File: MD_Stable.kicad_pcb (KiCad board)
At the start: 2 copper layers, 100 x 100 mm, 305 parts, among them J1 Conn_02x04_Counter_Clockwise, J10 Conn_02x06_Odd_Even, J11 Conn_01x08_Pin, J12 Conn_01x05_Socket, J2 XT30_Male, J3 XT60_Male, J4 RE1, J5 RE2, J6 RE3, J7 MO_XT60_Female1, J8 MO_XT60_Female2, J9 MO_XT60_Female3, Q1 TPH4R008QM, Q10 TPH4R008QM, Q11 TPH4R008QM, Q12 TPH4R008QM, Q2 TPH4R008QM, Q3 TPH4R008QM, Q4 TPH4R008QM, Q5 TPH4R008QM, Q6 TPH4R008QM, Q7 TPH4R008QM, Q8 TPH4R008QM, Q9 TPH4R008QM, SW1 SW_Push, SW2 SW_Push, SW3 PWM, SW4 PWM, SW5 PWM, SW6 DIR, SW7 DIR, SW8 DIR, U1 NJM7808SDL1, U10 74AHC1G08W5, U11 74AHC1G08W5, U12 74AHC1G08W5, U13 IRS2302S, U14 IRS2302S, U15 IRS2302S, U16 NE555D, U17 IRS2302S, U18 IRS2302S, U19 IRS2302S, U2 BA05CC0Tに似た何か, U20 74AHC1G08W5, U21 74AHC1G08W5, U22 74AHC1G08W5, U23 UTRS485G-S08-R, U24 UTRS485G-S08-R, U3 STM32G431K8Tx, U4 BA05CC0Tに似た何か, U5 BA033CC0FP, U6 π160M60, U7 74AHC1G04W5, U8 74AHC1G04W5, U9 74AHC1G04W5

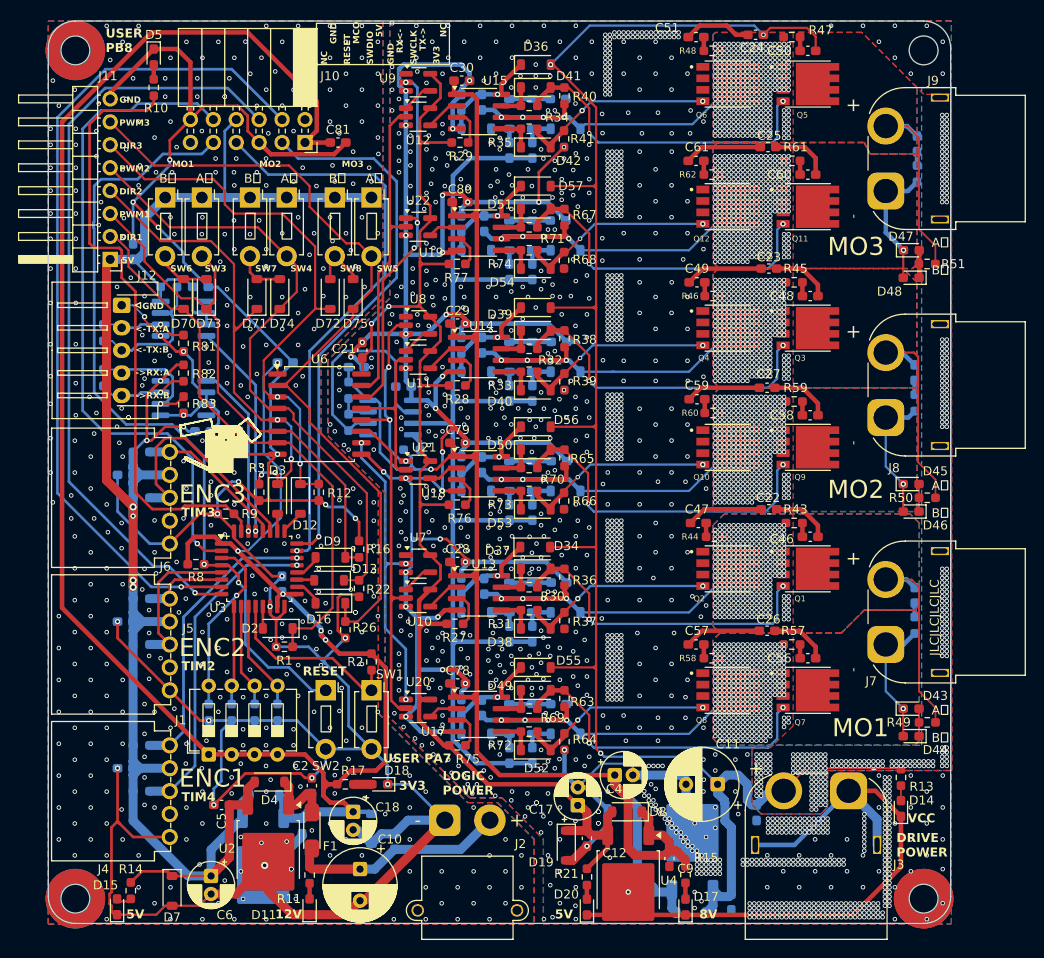
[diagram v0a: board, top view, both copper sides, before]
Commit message: 配線修正
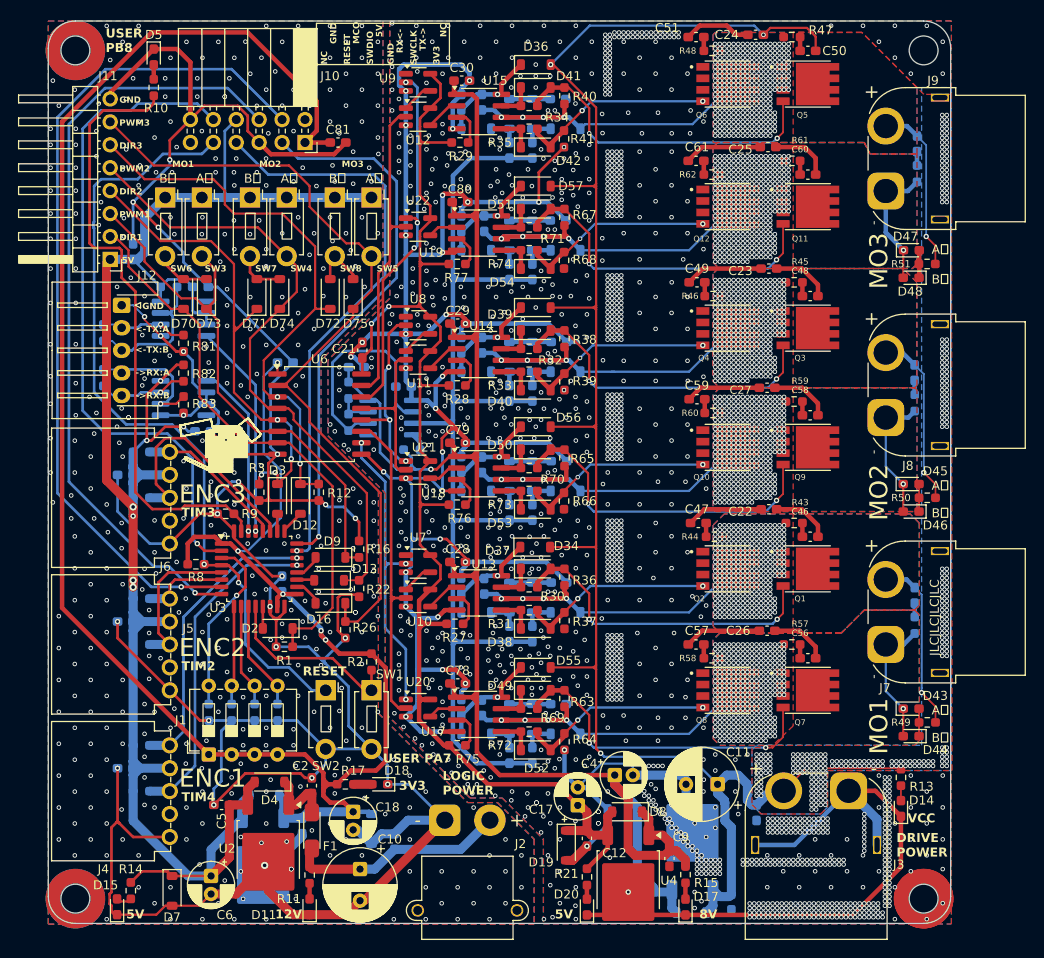
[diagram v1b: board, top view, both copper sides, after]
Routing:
- net Source_2A: track 63.7 -> 59.2 mm, vias 349 -> 342
- net Source_3A: track 62.0 -> 58.1 mm, vias 335 -> 327
- net Source_1A: track 62.5 -> 58.6 mm, vias 324 -> 317
- net Source_3B: vias 376 -> 369
- net Source_2B: vias 363 -> 356

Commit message: RS485Tx fix
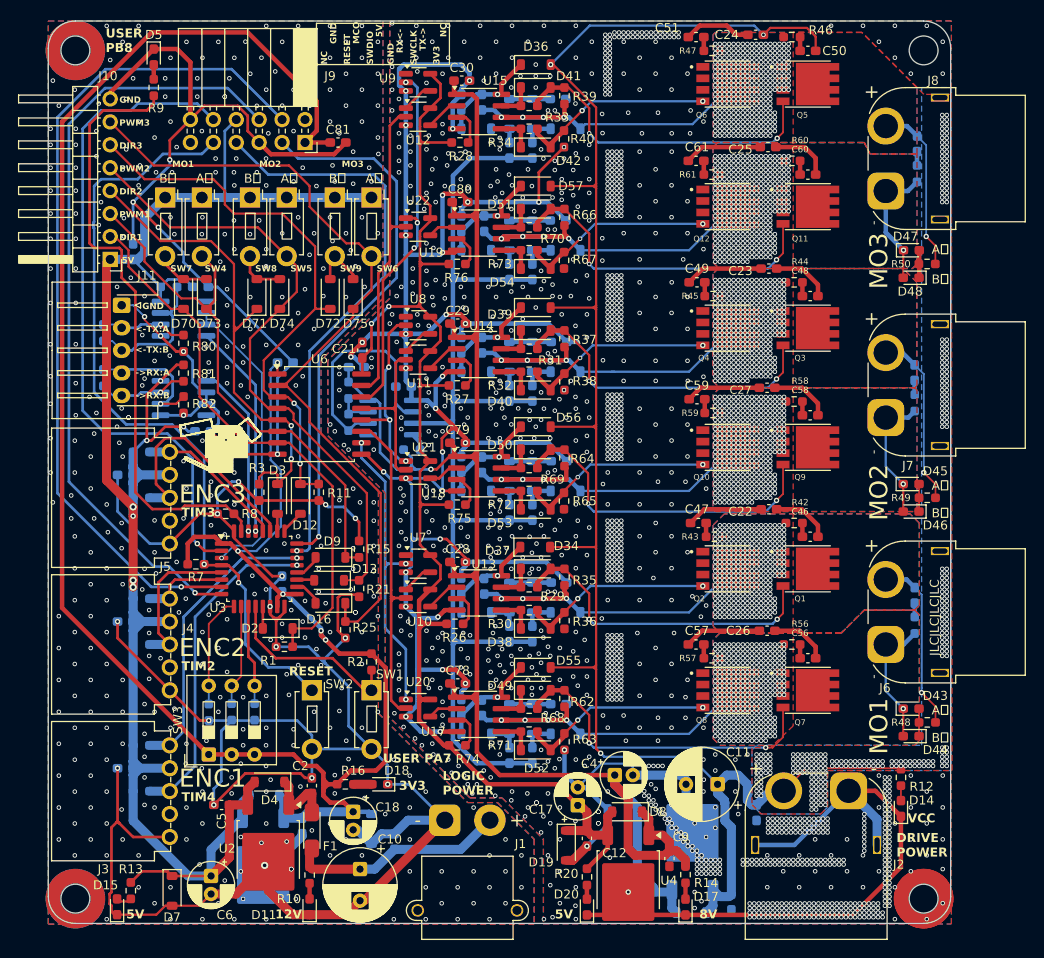
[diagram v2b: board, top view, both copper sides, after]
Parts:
- removed the J1 at (119.4, 132.1)
- removed the R7 at (119.4, 127.4)
- added SW3: SW_DIP_x03, Button_Switch_THT:SW_DIP_SPSTx03_Slide_9.78x9.8mm_W7.62mm_P2.54mm, F.Cu at (119.4, 132.1)
- moved R4 2.54 mm to (124.5, 127.4)
- moved R5 2.54 mm to (121.9, 127.4)
- moved R6 2.54 mm to (119.4, 127.4)
- moved SW2 1.52 mm to (130.8, 125.0)
- renumbered C84 to C82, C82 to C83, C83 to C84, J2 to J1, J11 to J10, J12 to J11, J3 to J2, J4 to J3, J5 to J4, J6 to J5, J7 to J6, J8 to J7, J9 to J8, J10 to J9, R11 to R10, R12 to R11, R13 to R12, R14 to R13, R15 to R14, R16 to R15, R17 to R16, R18 to R17, R19 to R18, R20 to R19, R21 to R20, R22 to R21, R23 to R22, R24 to R23, R25 to R24, R26 to R25, R27 to R26, R28 to R27, R29 to R28, R30 to R29, R31 to R30, R32 to R31, R33 to R32, R34 to R33, R35 to R34, R36 to R35, R37 to R36, R38 to R37, R39 to R38, R40 to R39, R41 to R40, R42 to R41, R43 to R42, R44 to R43, R45 to R44, R46 to R45, R47 to R46, R48 to R47, R49 to R48, R50 to R49, R51 to R50, R52 to R51, R53 to R52, R54 to R53, R55 to R54, R56 to R55, R57 to R56, R58 to R57, R59 to R58, R60 to R59, R61 to R60, R62 to R61, R63 to R62, R64 to R63, R65 to R64, R66 to R65, R67 to R66, R68 to R67, R69 to R68, R70 to R69, R8 to R7, R71 to R70, R72 to R71, R73 to R72, R74 to R73, R75 to R74, R76 to R75, R77 to R76, R78 to R77, R79 to R78, R80 to R79, R9 to R8, R81 to R80, R82 to R81, R83 to R82, R10 to R9, SW3 to SW4, SW4 to SW5, SW5 to SW6, SW6 to SW7, SW7 to SW8, SW8 to SW9
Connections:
- J1 pad : (no net) -> GNDD
- U23 pad 2: +5VD -> RS485_DE
- U23 pad 3: +5VD -> RS485_DE
- U3 pad 3: DIP_4 -> RS485_DE
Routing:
- net RS485_DE: track 0.00 -> 33.7 mm, vias 0 -> 1
- net DIP_4: track 19.8 -> 0.00 mm, vias 1 -> 0
- net GNDD: track 390.8 -> 384.1 mm, vias 445 -> 442
- net +5VD: track 216.2 -> 210.2 mm
- net DIP_3: track 10.9 -> 12.5 mm
- net RESET: track 88.5 -> 87.0 mm
- net DIP_1: track 12.1 -> 11.0 mm
- net DIR2: vias 4 -> 2
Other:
- board text added: "DCMotor Driver Rev3.2 @KayOChef_meme"
- board text removed: "DCMotor Driver Rev3.1 @KayOChef_meme"

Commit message: beyond the MD10C Rev4.0
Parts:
- Q1, Q10, Q11, Q12, Q2, Q3, Q4, Q5, Q6, Q7, Q8, Q9: value TPH4R008QM -> AGM028N08A; footprint MyLib:8-SOP Advance (5x5.75) -> Package_DFN_QFN:PQFN-8-EP_6x5mm_P1.27mm_Generic
- U1: value NJM7808SDL1 -> NJM7815SDL1
- U13, U14, U15, U17, U18, U19: value IRS2302S -> IR2184
- moved C28 8.24 mm to (151.5, 117.6), turned to 180 degrees
- moved C78 8.24 mm to (151.5, 131.1), turned to 180 degrees
- moved C79 8.19 mm to (151.0, 104.6), turned to 180 degrees
- moved C29 8.10 mm to (151.3, 91.2), turned to 180 degrees
- moved C80 7.97 mm to (151.3, 77.7), turned to 180 degrees
- moved C30 7.87 mm to (151.3, 64.3), turned to 180 degrees
- moved R28 3.56 mm to (143.7, 64.3)
- moved R27 3.25 mm to (143.7, 91.2)
- moved R75 3.25 mm to (143.7, 104.4)
- moved R76 3.25 mm to (143.7, 77.7)
- moved R26 3.00 mm to (143.7, 117.6)
- moved C23 0.76 mm to (180.7, 78.2)
- moved C25 0.66 mm to (180.7, 64.8)
- moved C26 0.56 mm to (180.7, 118.4)
- moved C27 0.56 mm to (180.7, 91.4)
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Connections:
- C28 pad 1: +8V -> +15V
- C29 pad 1: +8V -> +15V
- C3 pad 1: +8V -> +15V
- C30 pad 1: +8V -> +15V
- C4 pad 1: +8V -> +15V
- C62 pad 1: +8V -> +15V
- C78 pad 1: +8V -> +15V
- C79 pad 1: +8V -> +15V
- C80 pad 1: +8V -> +15V
- C9 pad 1: +8V -> +15V
- D1 pad 2: +8V -> +15V
- D6 pad 1: +8V -> +15V
- D8 pad 1: +8V -> +15V
- R14 pad 2: +8V -> +15V
- R41 pad 1: +8V -> +15V
- R54 pad 1: +8V -> +15V
- U1 pad 3: +8V -> +15V
- U13 pad 1: +8V -> Net-(U10A-Y)
- U13 pad 2: Net-(U10A-Y) -> Net-(U13-~{SD})
- U13 pad 3: Net-(U13-~{SD}) -> GND
- U13 pad 4: GND -> Net-(D38-K)
- U13 pad 5: Net-(D38-K) -> +15V
- U14 pad 1: +8V -> Net-(U11A-Y)
- U14 pad 2: Net-(U11A-Y) -> Net-(U14-~{SD})
- U14 pad 3: Net-(U14-~{SD}) -> GND
- U14 pad 4: GND -> Net-(D40-K)
- U14 pad 5: Net-(D40-K) -> +15V
- U15 pad 1: +8V -> Net-(U12A-Y)
- U15 pad 2: Net-(U12A-Y) -> Net-(U15-~{SD})
- U15 pad 3: Net-(U15-~{SD}) -> GND
- U15 pad 4: GND -> Net-(D42-K)
- U15 pad 5: Net-(D42-K) -> +15V
- U16 pad 8: +8V -> +15V
- U17 pad 1: +8V -> Net-(U17-IN)
- U17 pad 2: Net-(U17-IN) -> Net-(U17-~{SD})
- U17 pad 3: Net-(U17-~{SD}) -> GND
- U17 pad 4: GND -> Net-(D52-K)
- U17 pad 5: Net-(D52-K) -> +15V
- U18 pad 1: +8V -> Net-(U18-IN)
- U18 pad 2: Net-(U18-IN) -> Net-(U18-~{SD})
- U18 pad 3: Net-(U18-~{SD}) -> GND
- U18 pad 4: GND -> Net-(D53-K)
- U18 pad 5: Net-(D53-K) -> +15V
- U19 pad 1: +8V -> Net-(U19-IN)
- U19 pad 2: Net-(U19-IN) -> Net-(U19-~{SD})
- U19 pad 3: Net-(U19-~{SD}) -> GND
- U19 pad 4: GND -> Net-(D54-K)
- U19 pad 5: Net-(D54-K) -> +15V
- U4 pad 1: +8V -> +15V
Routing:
- net +15V: track 0.00 -> 247.3 mm, vias 0 -> 14
- net +8V: track 188.8 -> 0.00 mm, vias 1 -> 0
- net GND: track 402.6 -> 320.9 mm, vias 1305 -> 1261
- net +5V: track 150.8 -> 135.1 mm
- net Net-(D52-K): track 4.19 -> 11.3 mm
- net Net-(D54-K): track 4.19 -> 11.2 mm
- net Net-(D38-K): track 4.19 -> 11.0 mm
- net Net-(D53-K): track 4.19 -> 10.9 mm
- net Net-(D42-K): track 4.19 -> 10.7 mm
- net Net-(D40-K): track 4.19 -> 10.5 mm
- net VCC: track 231.4 -> 235.2 mm
- net 555_Out_A: track 126.3 -> 130.0 mm
- net Net-(U18-~{SD}): track 3.86 -> 5.62 mm
- net Net-(U19-~{SD}): track 3.88 -> 5.57 mm
- net Net-(U13-~{SD}): track 4.01 -> 5.62 mm
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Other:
- board text added: "DCMotor Driver Rev4.0 @KayOChef_meme"
- board text added: "MO0"
- board text removed: "DCMotor Driver Rev3.2 @KayOChef_meme"
